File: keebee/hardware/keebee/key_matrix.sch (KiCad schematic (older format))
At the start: 69 parts, among them SW1 SW_SPST, SW10 SW_SPST, SW11 SW_SPST, SW12 SW_SPST, SW13 SW_SPST, SW14 SW_SPST, SW15 SW_SPST, SW16 SW_SPST, SW17 SW_SPST, SW18 SW_SPST, SW19 SW_SPST, SW2 SW_SPST, SW20 SW_SPST, SW21 SW_SPST, SW22 SW_SPST, SW23 SW_SPST, SW24 SW_SPST, SW25 SW_SPST, SW26 SW_SPST, SW27 SW_SPST, SW28 SW_SPST, SW29 SW_SPST, SW3 SW_SPST, SW30 SW_SPST, SW31 SW_SPST, SW32 SW_SPST, SW33 SW_SPST, SW34 SW_SPST, SW35 SW_SPST, SW36 SW_SPST, SW37 SW_SPST, SW38 SW_SPST, SW39 SW_SPST, SW4 SW_SPST, SW40 SW_SPST, SW41 SW_SPST, SW42 SW_SPST, SW43 SW_SPST, SW44 SW_SPST, SW45 SW_SPST, SW46 SW_SPST, SW47 SW_SPST, SW48 SW_SPST, SW49 SW_SPST, SW5 SW_SPST, SW50 SW_SPST, SW51 SW_SPST, SW52 SW_SPST, SW53 SW_SPST, SW54 SW_SPST, SW55 SW_SPST, SW56 SW_SPST, SW57 SW_SPST, SW58 SW_SPST, SW59 SW_SPST, SW6 SW_SPST, SW60 SW_SPST, SW61 SW_SPST, SW62 SW_SPST, SW63 SW_SPST, SW64 SW_SPST, SW65 SW_SPST, SW66 SW_SPST, SW67 SW_SPST, SW68 SW_SPST, SW69 SW_SPST, SW7 SW_SPST, SW8 SW_SPST, SW9 SW_SPST

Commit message: Assign footprints and generate initial netlist.
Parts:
- SW1, SW10, SW11, SW12, SW13, SW14, SW15, SW16, SW17, SW18, SW19, SW2, SW20, SW21, SW22, SW23, SW24, SW25, SW26, SW27, SW28, SW29, SW3, SW30, SW31, SW32, SW33, SW34, SW36, SW37, SW38, SW39, SW4, SW40, SW41, SW42, SW43, SW44, SW45, SW46, SW47, SW48, SW49, SW5, SW50, SW51, SW52, SW53, SW54, SW55, SW56, SW57, SW58, SW59, SW6, SW60, SW61, SW62, SW63, SW64, SW65, SW66, SW67, SW68, SW69, SW7, SW8, SW9: footprint (none) -> Buttons_Switches_Keyboard:SW_Cherry_MX1A_1.00u_Plate
- SW35: footprint (none) -> Buttons_Switches_Keyboard:SW_Cherry_MX1A_2.00u_Plate

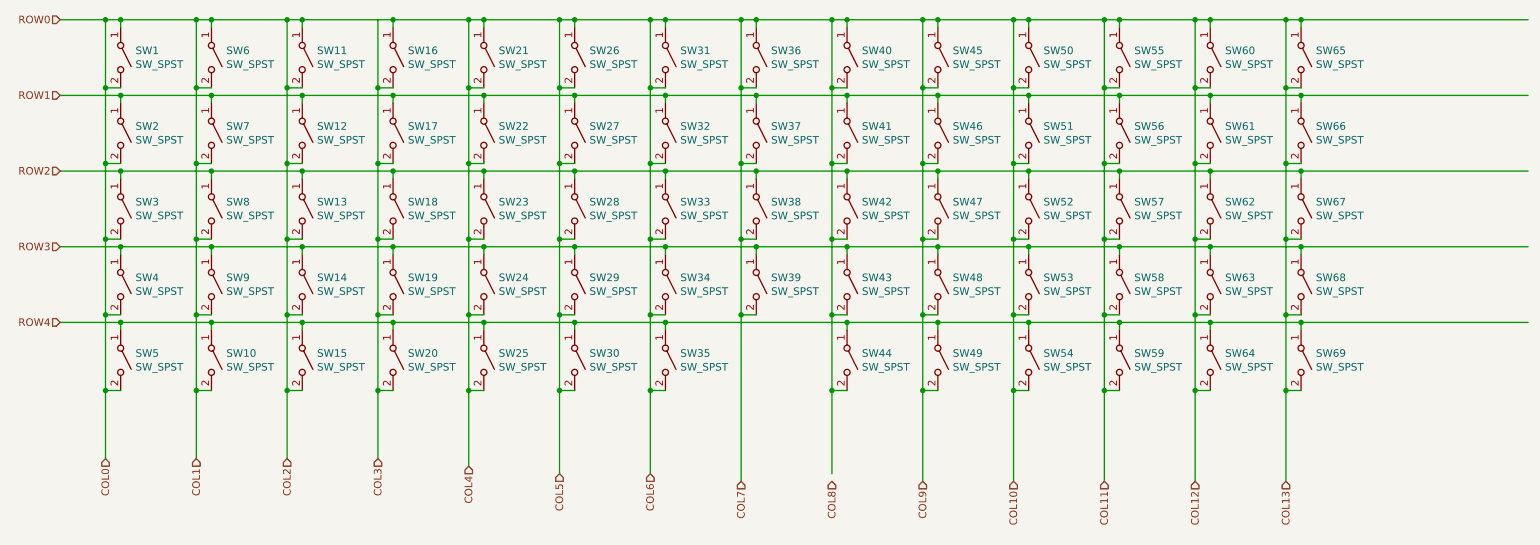
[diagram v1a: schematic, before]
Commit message: Add diodes to the key matrix
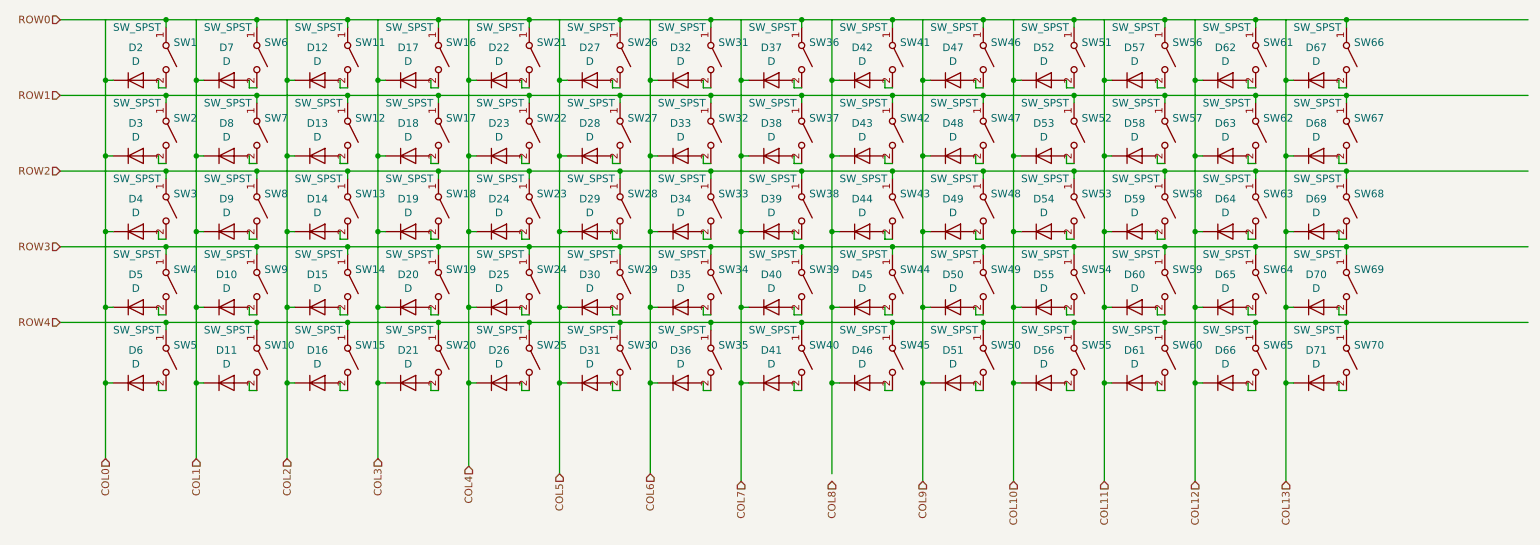
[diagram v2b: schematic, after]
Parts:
- added D10, D11, D12, D13, D14, D15, D16, D17, D18, D19, D2, D20, D21, D22, D23, D24, D25, D26, D27, D28, D29, D3, D30, D31, D32, D33, D34, D35, D36, D37, D38, D39, D4, D40, D41, D42, D43, D44, D45, D46, D47, D48, D49, D5, D50, D51, D52, D53, D54, D55, D56, D57, D58, D59, D6, D60, D61, D62, D63, D64, D65, D66, D67, D68, D69, D7, D70, D71, D8, D9: D, symbol Device:D
- added SW70: SW_SPST, Buttons_Switches_Keyboard:SW_Cherry_MX1A_1.00u_Plate, symbol Switch:SW_SPST
- SW35: footprint Buttons_Switches_Keyboard:SW_Cherry_MX1A_2.00u_Plate -> Buttons_Switches_Keyboard:SW_Cherry_MX1A_1.00u_Plate
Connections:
- wire segments 308 -> 439
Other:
- moved on the sheet: SW1

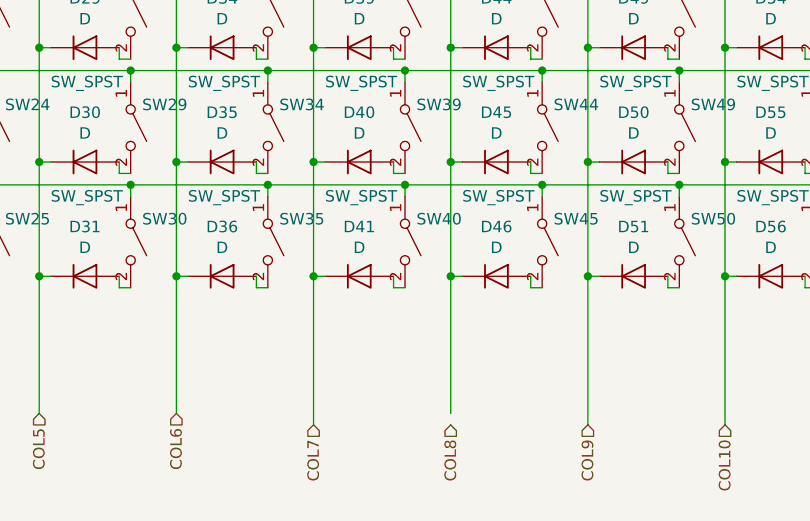
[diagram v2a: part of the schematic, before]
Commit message: Remove extra spacebar switch.
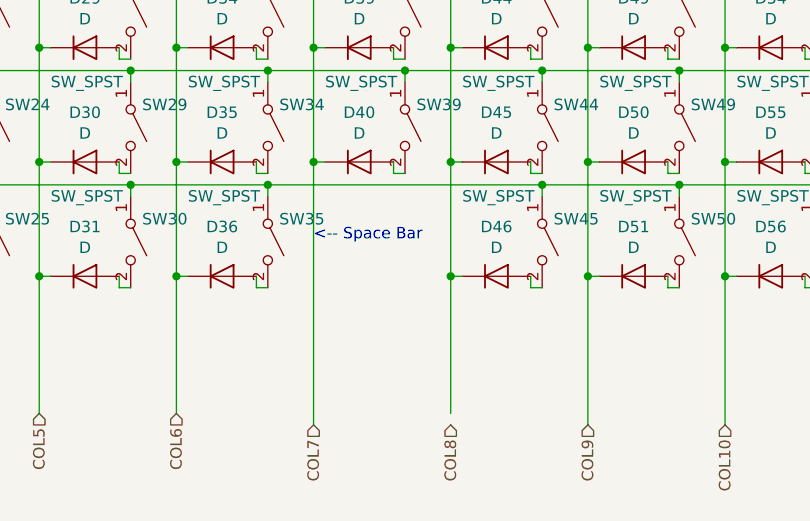
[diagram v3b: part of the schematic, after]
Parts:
- removed D41: D, symbol Device:D
- removed SW40: SW_SPST, Buttons_Switches_Keyboard:SW_Cherry_MX1A_1.00u_Plate, symbol Switch:SW_SPST
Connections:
- wire segments 439 -> 433
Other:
- note added: "<-- Space Bar"
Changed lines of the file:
@@
-	0    1    1    0
-$EndComp
-$Comp
-L Device:D D41
-U 1 1 5BCD2582
-P 5950 4350
-F 0 "D41" H 5950 4566 50  0000 C CNN
-F 1 "D" H 5950 4475 50  0000 C CNN
-F 2 "" H 5950 4350 50  0001 C CNN
-F 3 "~" H 5950 4350 50  0001 C CNN
-	1    5950 4350
-	1    0    0    -1
-$EndComp
-Wire Wire Line
-	6150 4400 6100 4400
-Wire Wire Line
-	6100 4400 6100 4350
-Wire Wire Line
-	5800 4350 5750 4350
-Wire Wire Line
-	6150 4000 6150 3950
-$Comp
-L Switch:SW_SPST SW40
-U 1 1 5BCD258D
-P 6150 4200
-F 0 "SW40" V 6050 4250 50  0000 L CNN
-F 1 "SW_SPST" V 5950 3850 50  0000 L CNN
-F 2 "Buttons_Switches_Keyboard:SW_Cherry_MX1A_1.00u_Plate" H 6150 4200 50  0001 C CNN
-F 3 "" H 6150 4200 50  0001 C CNN
-	1    6150 4200
 	0    1    1    0
 $EndComp
@@
 	5150 4350 5150 4950
 Connection ~ 5550 3950
-Wire Wire Line
-	5550 3950 6150 3950
 Connection ~ 5150 3850
 Wire Wire Line
@@
 	6150 3450 6750 3450
 Connection ~ 5750 3850
-Wire Wire Line
-	5750 3850 5750 4350
-Connection ~ 6150 3950
-Wire Wire Line
-	6150 3950 6750 3950
-Connection ~ 5750 4350
-Wire Wire Line
-	5750 4350 5750 5000
 Connection ~ 6350 4350
 Wire Wire Line
@@
 Wire Wire Line
 	1250 1950 1950 1950
+Wire Wire Line
+	5750 3850 5750 5000
+Wire Wire Line
+	5550 3950 6750 3950
+Text Notes 5750 4200 0    50   ~ 0
+<-- Space Bar
 $EndSCHEMATC

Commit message: Add Diode footprints
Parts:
- D10, D11, D12, D13, D14, D15, D16, D17, D18, D19, D2, D20, D21, D22, D23, D24, D25, D26, D27, D28, D29, D3, D30, D31, D32, D33, D34, D35, D36, D37, D38, D39, D4, D40, D42, D43, D44, D45, D46, D47, D48, D49, D5, D50, D51, D52, D53, D54, D55, D56, D57, D58, D59, D6, D60, D61, D62, D63, D64, D65, D66, D67, D68, D69, D7, D70, D71, D8, D9: footprint (none) -> Diodes_SMD:D_SOD-123

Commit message: Relabel components
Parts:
- SW35: footprint Buttons_Switches_Keyboard:SW_Cherry_MX1A_1.00u_Plate -> Buttons_Switches_Keyboard:SW_Cherry_MX1A_2.00u_Plate
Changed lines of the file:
@@
 F 0 "SW35" V 5450 4250 50  0000 L CNN
 F 1 "SW_SPST" V 5350 3850 50  0000 L CNN
-F 2 "Buttons_Switches_Keyboard:SW_Cherry_MX1A_1.00u_Plate" H 5550 4200 50  0001 C CNN
+F 2 "Buttons_Switches_Keyboard:SW_Cherry_MX1A_2.00u_Plate" H 5550 4200 50  0001 C CNN
 F 3 "" H 5550 4200 50  0001 C CNN
 	1    5550 4200

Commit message: Route more trackes.
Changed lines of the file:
@@
 Text HLabel 5750 5000 3    50   Input ~ 0
 COL7
-Text HLabel 6350 5000 3    50   Input ~ 0
+Text HLabel 6350 4950 3    50   Input ~ 0
 COL8
 Text HLabel 6950 5000 3    50   Input ~ 0
